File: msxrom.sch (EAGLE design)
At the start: 9 parts

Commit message: with io breakout
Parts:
- added JP10, JP11, JP12, JP13, JP15, JP16: (no value), pinhead-round:PINHD-1X1
- added JP14, JP17, JP18, JP9: (no value), pinhead-round:PINHD-1X4
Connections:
- new net !IORQ: JP1.!IORQ, JP11.1
- new net !RD: JP1.!RD, JP13.1, JP16.1
- new net !WAIT: JP1.!WAIT, JP10.1
- new net !WR: JP1.!WR, JP12.1, JP15.1
- new net N$9: JP1.SW@1, JP1.SW@2
- net A0: now also JP17.1
- net A1: now also JP17.2
- net A2: now also JP17.3
- net N$1: now also JP9.1
- net N$13: now also JP18.4
- net N$14: now also JP18.3
- net N$15: now also JP18.2
- net N$16: now also JP18.1
- net N$17: now also JP17.4
- net N$2: now also JP9.2
- net N$3: now also JP9.3
- net N$4: now also JP9.4
- net N$5: now also JP14.1
- net N$6: now also JP14.2
- net N$7: now also JP14.3
- net N$8: now also JP14.4
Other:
- moved on the sheet: IC1

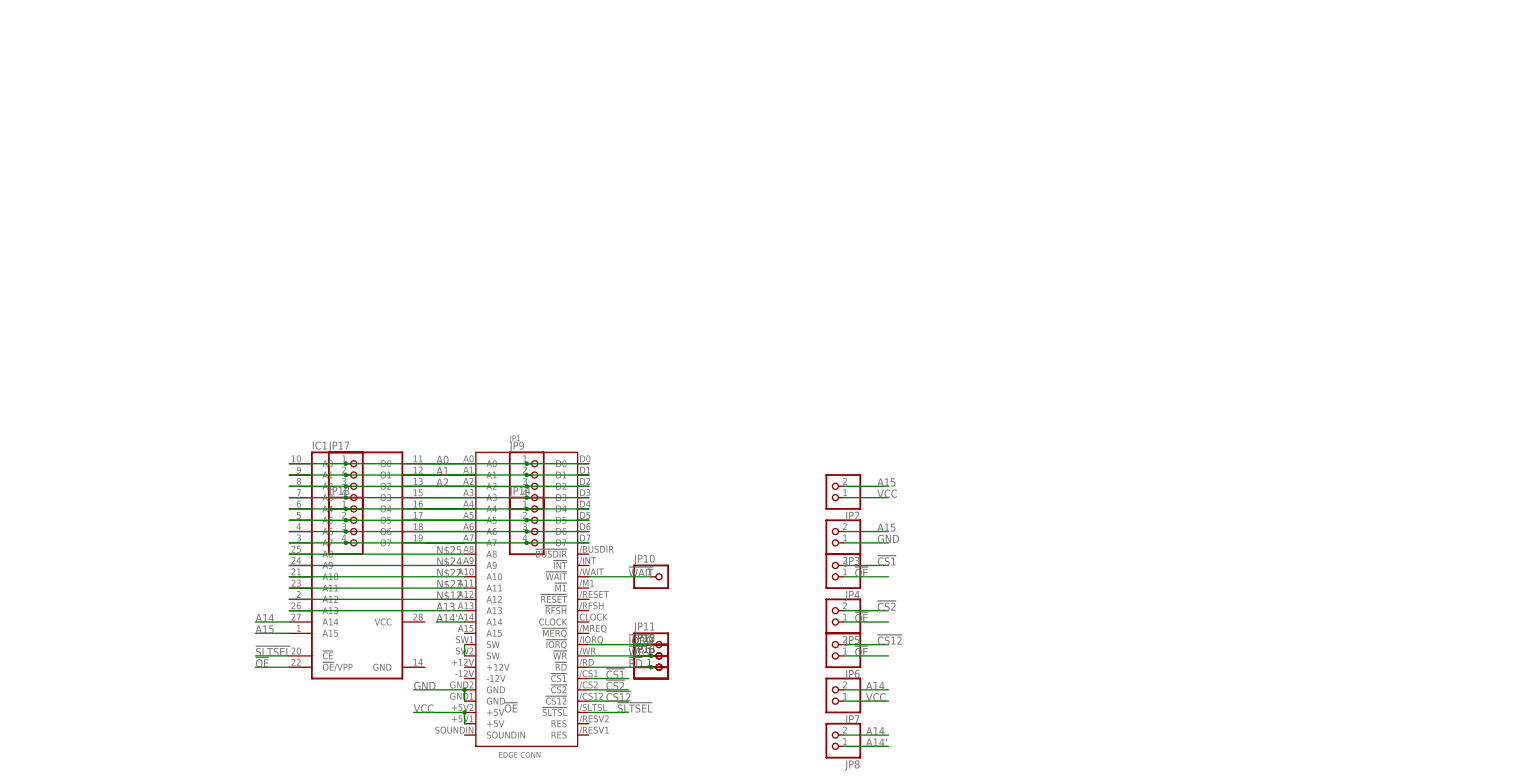
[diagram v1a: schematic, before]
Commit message: finished board but eagle broke something...
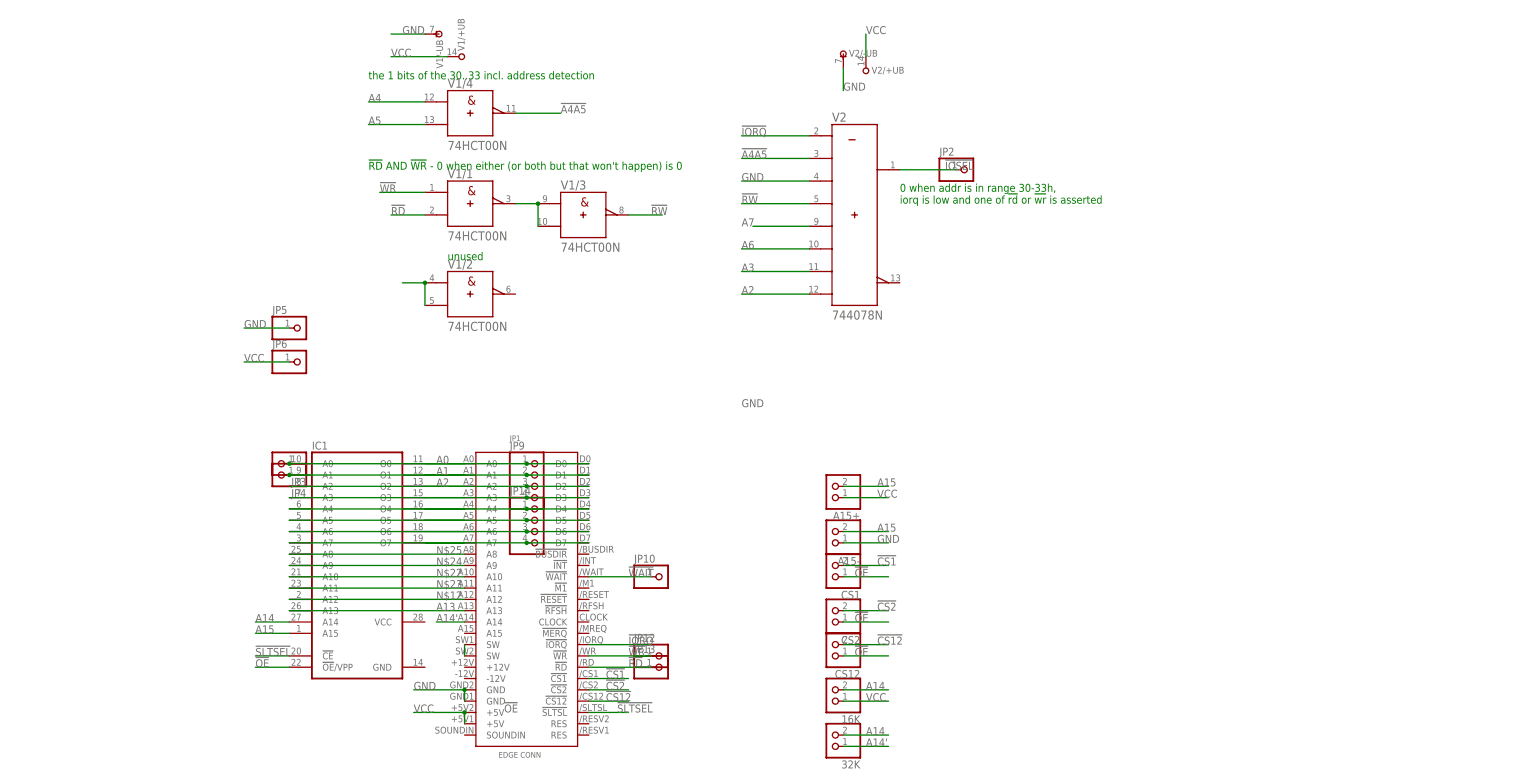
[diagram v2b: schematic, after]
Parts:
- removed JP11, JP15, JP16: (no value), pinhead-round:PINHD-1X1
- removed JP17, JP18: (no value), pinhead-round:PINHD-1X4
- added A15+, A15-, CS1, CS12, CS2: (no value), pinhead-round:PINHD-1X2
- added V1: 74HCT00N, 74ttl-din:74HCT00N
- added V2: 744078N, 74ttl-din:744078N
- JP2, JP3, JP4, JP5, JP6: device pinhead-round:PINHD-1X2 -> pinhead-round:PINHD-1X1
- renumbered JP7 to 16K, JP8 to 32K
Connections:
- removed net N$13: IC1.A7, JP1.A7, JP18.4
- removed net N$14: IC1.A6, JP1.A6, JP18.3
- removed net N$15: IC1.A5, JP1.A5, JP18.2
- removed net N$16: IC1.A4, JP1.A4, JP18.1
- removed net N$17: IC1.A3, JP1.A3, JP17.4
- new net !A4A5: V1/4.Y, V21.B
- new net !IOSEL: JP2.1, V21.Y
- new net !RW: V1/3.Y, V21.D
- new net A3: IC1.A3, JP1.A3, V21.G
- new net A4: IC1.A4, JP1.A4, V1/4.A
- new net A5: IC1.A5, JP1.A5, V1/4.B
- new net A6: IC1.A6, JP1.A6, V21.F
- new net A7: IC1.A7, JP1.A7, V21.E
- new net N$10: V1/1.Y, V1/3.A, V1/3.B
- net !CS1: now also CS1.2; no longer JP4.2
- net !CS12: now also CS12.2; no longer JP6.2
- net !CS2: now also CS2.2; no longer JP5.2
- net !IORQ: now also V21.A; no longer JP11.1
- net !OE: now also CS1.1, CS12.1, CS2.1; no longer JP4.1, JP5.1, JP6.1
- net !RD: now also V1/1.B; no longer JP16.1
- net !WR: now also V1/1.A; no longer JP15.1
- net A0: now also JP3.1; no longer JP17.1
- net A1: now also JP4.1; no longer JP17.2
- net A15: now also A15+.2, A15-.2; no longer JP2.2, JP3.2
- net A2: now also V21.H; no longer JP17.3
- net GND: now also A15-.1, JP5.1, V1/-UB.-UB, V1/2.A, V1/2.B, V2/-UB.-UB, V21.C; no longer JP3.1
- net VCC: now also A15+.1, JP6.1, V1/+UB.+UB, V2/+UB.+UB; no longer JP2.1
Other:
- note added: "!RD! AND !WR! - 0 when either (or both but that won't happen) is 0"
- note added: "0 when addr is in range 30-33h, iorq is low and one of !rd! or !wr! is asserted"
- note added: "the 1 bits of the 30..33 incl. address detection"
- note added: "unused"

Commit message: with sdx connector and branding
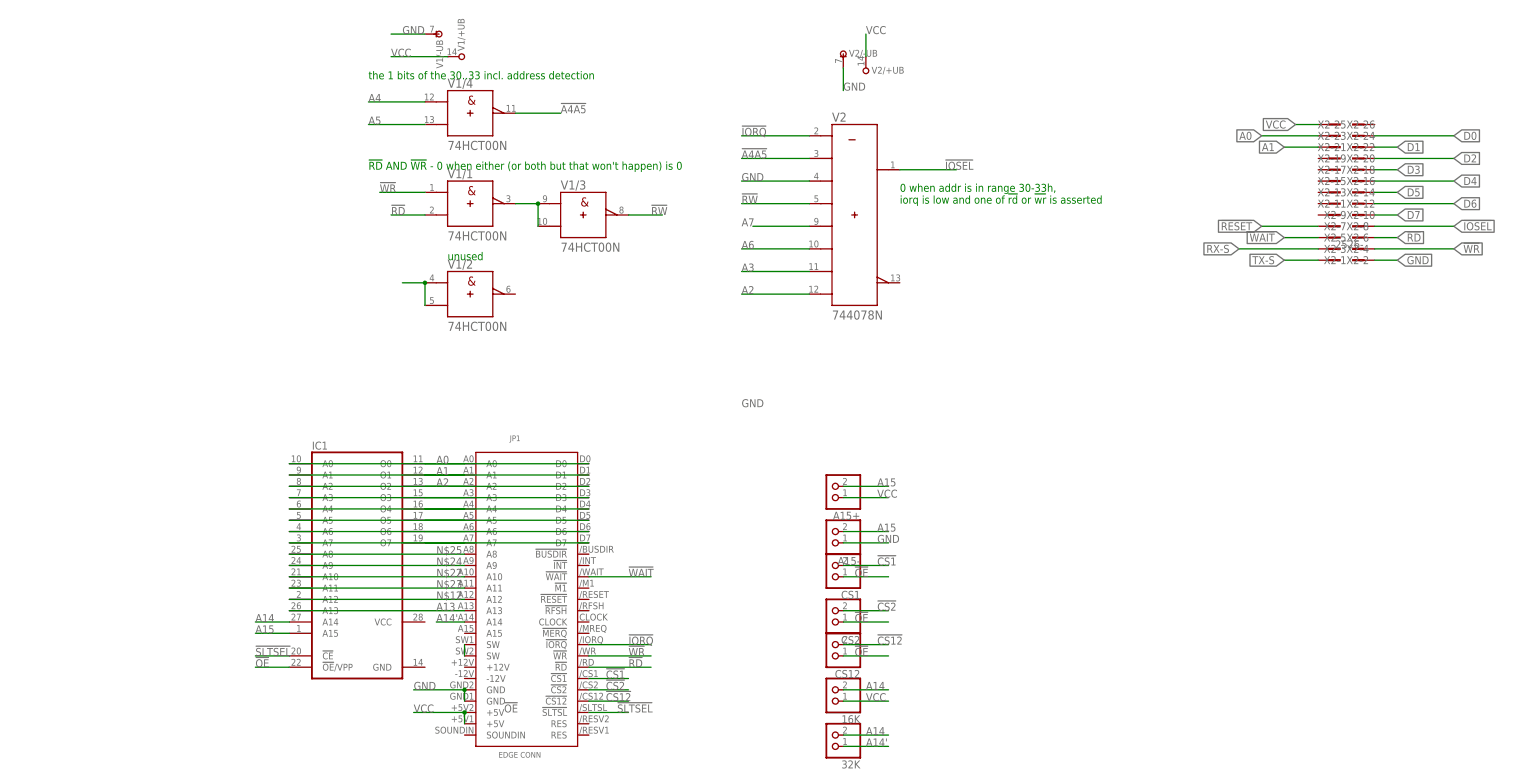
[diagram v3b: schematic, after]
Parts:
- removed JP10, JP12, JP13, JP2, JP3, JP4, JP5, JP6: (no value), pinhead-round:PINHD-1X1
- removed JP14, JP9: (no value), pinhead-round:PINHD-1X4
- added X2: 2526-, con-3m:2526-
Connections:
- removed net N$1: IC1.O0, JP1.D0, JP9.1
- removed net N$2: IC1.O1, JP1.D1, JP9.2
- removed net N$3: IC1.O2, JP1.D2, JP9.3
- removed net N$4: IC1.O3, JP1.D3, JP9.4
- removed net N$5: IC1.O4, JP1.D4, JP14.1
- removed net N$6: IC1.O5, JP1.D5, JP14.2
- removed net N$7: IC1.O6, JP1.D6, JP14.3
- removed net N$8: IC1.O7, JP1.D7, JP14.4
- new net !RESET: X2-8.KL
- new net D0: IC1.O0, JP1.D0, X2-23.KL
- new net D1: IC1.O1, JP1.D1, X2-21.KL
- new net D2: IC1.O2, JP1.D2, X2-19.KL
- new net D3: IC1.O3, JP1.D3, X2-17.KL
- new net D4: IC1.O4, JP1.D4, X2-15.KL
- new net D5: IC1.O5, JP1.D5, X2-13.KL
- new net D6: IC1.O6, JP1.D6, X2-11.KL
- new net D7: IC1.O7, JP1.D7, X2-9.KL
- new net RX-S: X2-4.KL
- new net TX-S: X2-2.KL
- net !IOSEL: now also X2-7.KL; no longer JP2.1
- net !RD: now also X2-5.KL; no longer JP13.1
- net !WAIT: now also X2-6.KL; no longer JP10.1
- net !WR: now also X2-3.KL; no longer JP12.1
- net A0: now also X2-24.KL; no longer JP3.1
- net A1: now also X2-22.KL; no longer JP4.1
- net GND: now also X2-1.KL; no longer JP5.1
- net VCC: now also X2-26.KL; no longer JP6.1

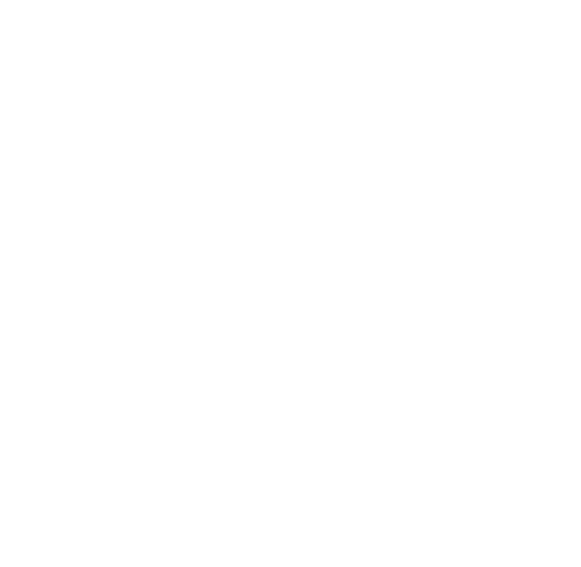
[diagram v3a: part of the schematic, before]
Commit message: msxrom as produced
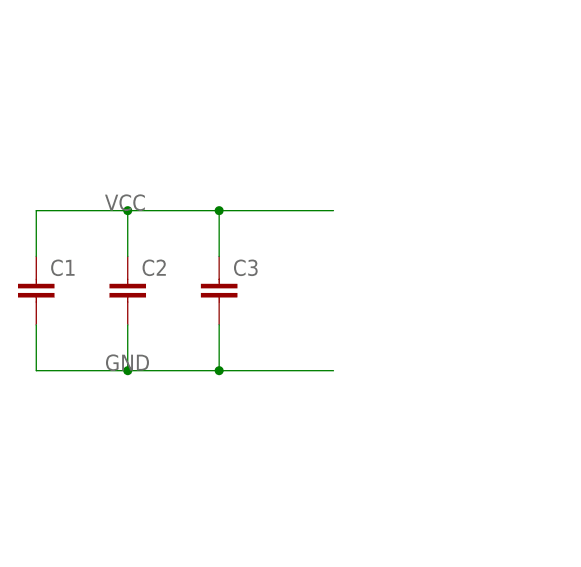
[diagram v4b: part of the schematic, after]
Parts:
- added C1, C2, C3: (no value), rcl:C-EU050-025X075
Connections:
- net GND: now also C1.2, C2.2, C3.2
- net VCC: now also C1.1, C2.1, C3.1
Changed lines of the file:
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@@
 <part name="V2" library="74ttl-din" library_urn="urn:adsk.eagle:library:84" deviceset="74*4078" device="N" package3d_urn="urn:adsk.eagle:package:1461/1"/>
 <part name="X2" library="con-3m" deviceset="2526-" device=""/>
+<part name="C1" library="rcl" deviceset="C-EU" device="050-025X075"/>
+<part name="C2" library="rcl" deviceset="C-EU" device="050-025X075"/>
+<part name="C3" library="rcl" deviceset="C-EU" device="050-025X075"/>
 </parts>
 <sheets>
@@
 <instance part="X2" gate="-25" x="200.66" y="162.56"/>
 <instance part="X2" gate="-26" x="198.12" y="162.56" rot="R180"/>
+<instance part="C1" gate="G$1" x="-99.06" y="91.44"/>
+<instance part="C2" gate="G$1" x="-88.9" y="91.44"/>
+<instance part="C3" gate="G$1" x="-78.74" y="91.44"/>
 </instances>
 <busses>
@@
 <wire x1="193.04" y1="162.56" x2="187.96" y2="162.56" width="0.1524" layer="91"/>
 </segment>
+<segment>
+<pinref part="C1" gate="G$1" pin="1"/>
+<wire x1="-99.06" y1="93.98" x2="-99.06" y2="99.06" width="0.1524" layer="91"/>
+<wire x1="-99.06" y1="99.06" x2="-88.9" y2="99.06" width="0.1524" layer="91"/>
+<pinref part="C2" gate="G$1" pin="1"/>
+<wire x1="-88.9" y1="99.06" x2="-78.74" y2="99.06" width="0.1524" layer="91"/>
+<wire x1="-78.74" y1="99.06" x2="-66.04" y2="99.06" width="0.1524" layer="91"/>
+<wire x1="-88.9" y1="93.98" x2="-88.9" y2="99.06" width="0.1524" layer="91"/>
+<junction x="-88.9" y="99.06"/>
+<pinref part="C3" gate="G$1" pin="1"/>
+<wire x1="-78.74" y1="93.98" x2="-78.74" y2="99.06" width="0.1524" layer="91"/>
+<junction x="-78.74" y="99.06"/>
+<label x="-91.44" y="99.06" size="1.778" layer="95"/>
+</segment>
 </net>
 <net name="GND" class="0">
@@
 <wire x1="205.74" y1="132.08" x2="210.82" y2="132.08" width="0.1524" layer="91"/>
 </segment>
-</net>
+<segment>
+<pinref part="C1" gate="G$1" pin="2"/>
+<wire x1="-99.06" y1="86.36" x2="-99.06" y2="81.28" width="0.1524" layer="91"/>
+<wire x1="-99.06" y1="81.28" x2="-88.9" y2="81.28" width="0.1524" layer="91"/>
+<pinref part="C2" gate="G$1" pin="2"/>
+<wire x1="-88.9" y1="81.28" x2="-78.74" y2="81.28" width="0.1524" layer="91"/>
+<wire x1="-78.74" y1="81.28" x2="-66.04" y2="81.28" width="0.1524" layer="91"/>
+<wire x1="-88.9" y1="86.36" x2="-88.9" y2="81.28" width="0.1524" layer="91"/>
+<junction x="-88.9" y="81.28"/>
+<pinref part="C3" gate="G$1" pin="2"/>
+<wire x1="-78.74" y1="86.36" x2="-78.74" y2="81.28" width="0.1524" layer="91"/>
+<junction x="-78.74" y="81.28"/>
+<label x="-91.44" y="81.28" size="1.778" layer="95"/>
+</segment>
+</net>
